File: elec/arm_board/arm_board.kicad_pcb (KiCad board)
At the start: 2 copper layers, 82.4 x 40.4 mm, 48 parts, among them J1 PinHeader, J12 B2B-XH-A(LF)(SN), J16 B4B-ZR(LF)(SN), J2 PinHeader, J3 B6B-ZR, J4 Fan motor, J5 Fan motor, J6 B2B-XH-A(LF)(SN), Q5 DMT6008LFG, SW1 B3U-3000P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

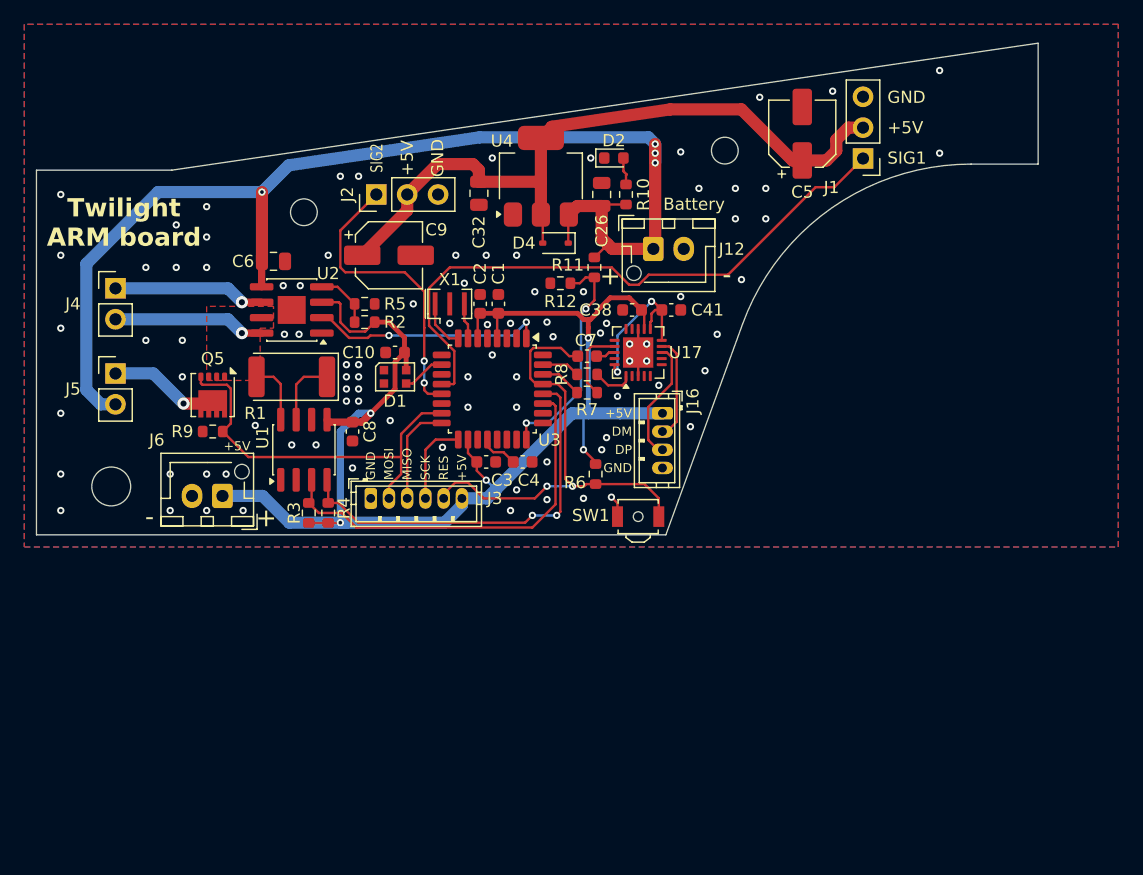
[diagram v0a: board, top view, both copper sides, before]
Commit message: アーム基板v2の回路図＆アートワーク
Signed-off-by: Kazuki Iida <elkel53930@gmail.com>
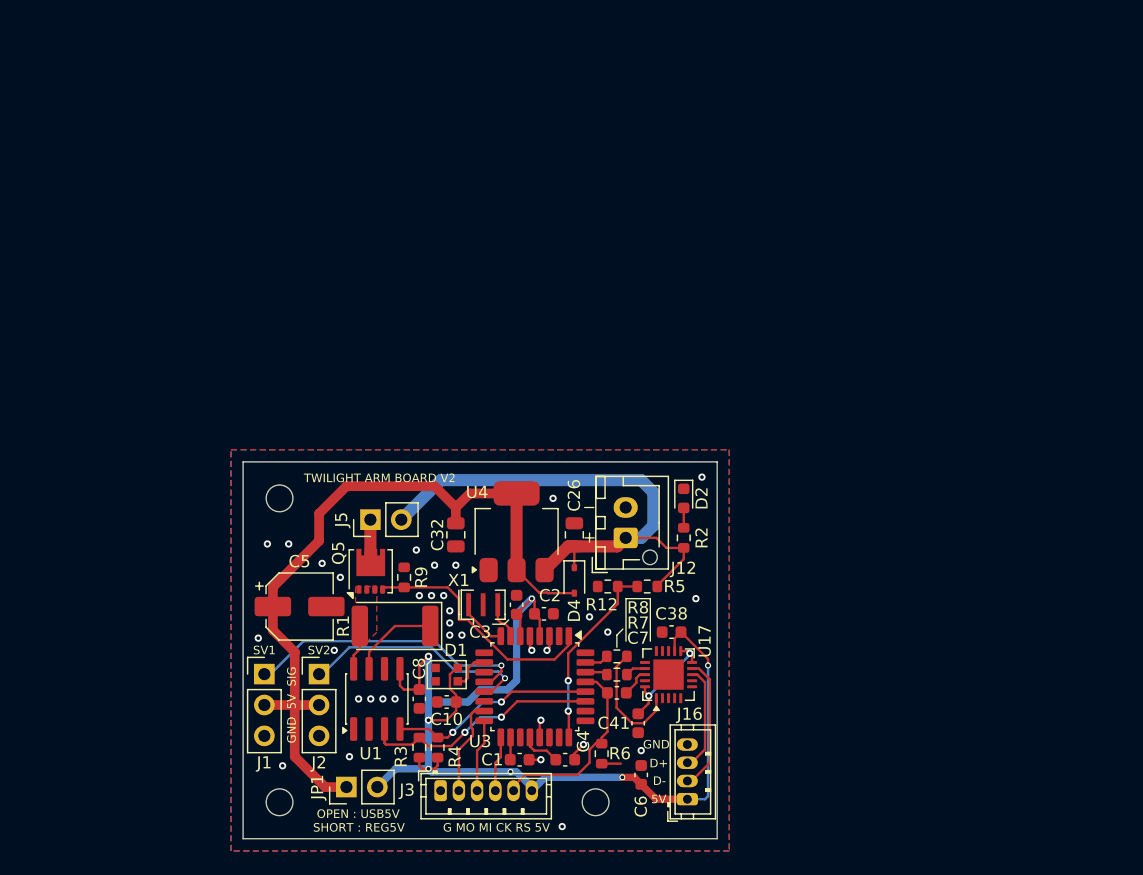
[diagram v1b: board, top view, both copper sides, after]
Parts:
- removed C9: RVT1A101M0505, Capacitor_SMD:CP_Elec_5x5.4
- removed J4: Fan motor, Connector_PinHeader_2.54mm:PinHeader_1x02_P2.54mm_Vertical
- removed J6: B2B-XH-A(LF)(SN), Connector_JST:JST_XH_B2B-XH-AM_1x02_P2.50mm_Vertical
- removed R10, R11: 0603WAF1002T5E, Resistor_SMD:R_0603_1608Metric
- removed SW1: B3U-3000P, Button_Switch_SMD:SW_SPST_B3U-3000P-B
- removed U2: TB67H450, Package_SO:HSOP-8-1EP_3.9x4.9mm_P1.27mm_EP2.3x2.3mm
- added JP1: Switch 5V supply, Connector_PinHeader_2.54mm:PinHeader_1x02_P2.54mm_Vertical, F.Cu at (135.5, 108.8)
- C6: value CL21A106KAYNNNE -> CL10A475KO8NNNC; footprint Capacitor_SMD:C_0805_2012Metric -> Capacitor_SMD:C_0603_1608Metric
- H3: value M3 -> M2; footprint MountingHole:MountingHole_3.2mm_M3 -> MountingHole:MountingHole_2.2mm_M2
- R5: value 0603WAF3901T5E -> 0603WAF1002T5E
- moved J1 65.0 mm to (128.8, 99.5), turned to 0 degrees
- moved C5 56.8 mm to (131.7, 93.9), turned to 0 degrees
- moved H1 54.7 mm to (156.0, 110.0)
- moved C6 52.0 mm to (159.8, 107.8), turned to 90 degrees
- moved J2 39.7 mm to (133.2, 99.5), turned to 0 degrees
- moved C1 37.5 mm to (149.8, 106.5), turned to 180 degrees
- moved C41 34.1 mm to (159.5, 103.5), turned to 90 degrees
- moved R5 32.9 mm to (160.2, 92.2), turned to 0 degrees
- moved J16 31.8 mm to (163.6, 109.8), turned to 90 degrees
- moved R2 31.7 mm to (163.2, 88.2), turned to -90 degrees
- moved H3 29.4 mm to (130.0, 110.0)
- moved U4 29.3 mm to (149.5, 87.8)
- moved C10 29.1 mm to (143.8, 101.8)
- moved D2 28.6 mm to (163.2, 85.0), turned to -90 degrees
- moved C32 28.2 mm to (144.5, 88.0)
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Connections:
- net /RS renamed Net-(U1-IN+)
- C6 pad 1: GND -> +5V
- C6 pad 2: +BATT -> GND
- Q5 pad 4: /MOSI -> /MOT_PWM
- R2 pad 1: Net-(U2-VREF) -> Net-(D2-A)
- R2 pad 2: +5V -> +BATT
- R5 pad 1: GND -> /VMON
- R5 pad 2: Net-(U2-VREF) -> +BATT
- R9 pad 2: /MOSI -> /MOT_PWM
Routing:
- net +BATT: track 98.1 -> 46.6 mm, vias 4 -> 0
- net /SERVO_SIG1: track 51.1 -> 23.7 mm, vias 0 -> 1
- net /MOSI: track 32.3 -> 8.03 mm
- net /RESET: track 39.4 -> 16.3 mm, vias 2 -> 0
- net +5V: track 116.2 -> 97.1 mm, vias 5 -> 7
- net /SCL: track 33.0 -> 17.1 mm
- net /SDA: track 33.1 -> 19.8 mm, vias 0 -> 2
- net Net-(J4-Pin_2): track 12.5 -> 0.00 mm, vias 1 -> 0
- net Net-(J4-Pin_1): track 12.5 -> 0.00 mm, vias 1 -> 0
- net /TX: track 3.33 -> 9.83 mm
- net /SERVO_SIG2: track 24.6 -> 19.4 mm, vias 2 -> 1
- net Net-(J5-Pin_1): track 9.13 -> 4.07 mm, vias 1 -> 0
- net Net-(U2-VREF): track 4.78 -> 0.00 mm
- net +5VA: track 58.8 -> 63.6 mm
- net /RX: track 6.18 -> 1.69 mm
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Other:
- board size 82.4 x 40.4 mm -> 39 x 31 mm
- board text added: "5V"
- board text added: "D+"
- board text added: "D-"
- board text added: "G MO MI CK RS 5V"
- board text added: "GND 5V SIG"
- board text added: "OPEN : USB5V SHORT : REG5V"
- board text added: "SV1"
- board text added: "SV2"
- board text added: "TWILIGHT ARM BOARD V2"
- board text removed: "+"
- board text removed: "+5V"
- board text removed: "-"
- board text removed: "Battery"
- board text removed: "DM"
- board text removed: "DP"
- board text removed: "MISO"
- board text removed: "MOSI"
- board text removed: "RES"
- board text removed: "SCK"
- board text removed: "SIG1"
- board text removed: "SIG2"
- board text removed: "Twilight ARM board"
